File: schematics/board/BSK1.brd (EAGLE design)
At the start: 82 x 100 mm, 70 parts

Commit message: Исправлена БСК1
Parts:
- added R24, R25: 2k26, resistor:R0603
- R1, R2: value 2k26 -> 200k
- R3, R5: value 1M -> 100R
- R4, R7: value 2M -> 100k
- moved R1 2.40 mm to (66.8, 51.1)
- moved R2 2.40 mm to (66.8, 53.5)
- moved U$57 0.32 mm to (58.6, 3.20), turned to 270 degrees
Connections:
- new net N$25: R1.2, R24.1, U$22.1
- new net N$26: R2.2, R25.1, U$22.3
- net 3V3: now also U$57.4, U$57.7; no longer U$57.5
- net B1-KVCC: now also R24.2, R25.2; no longer R1.2, R2.2, U$22.1, U$22.3
- net GND: now also U$57.3, U$57.8; no longer U$57.1, U$57.2, U$57.6
- net N$150: now also U$57.1; no longer U$57.8
- net N$151: now also U$57.2; no longer U$57.7
- net SCL-INA: now also U$57.5; no longer U$57.4
- net SDA-INA: now also U$57.6; no longer U$57.3
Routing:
- net 3V3: track 183.2 -> 197.9 mm, vias 7 -> 9
- net N$25: track 0.00 -> 13.2 mm
- net GND: track 69.4 -> 59.0 mm, vias 2 -> 0
- net N$26: track 0.00 -> 4.90 mm
- net B1-KVCC: track 85.9 -> 81.1 mm
- net SCL-INA: track 11.2 -> 8.40 mm
- net SP+: track 35.1 -> 33.1 mm, vias 0 -> 1
- net N$151: track 5.94 -> 7.75 mm
- net PL5-KVCC: track 128.9 -> 130.5 mm
- net SDA-INA: track 7.90 -> 6.74 mm
- net N$150: track 5.59 -> 6.15 mm

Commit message: Плата АB+DC-DC
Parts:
- moved R3 1.10 mm to (72.3, 54.2)
- moved R4 1.10 mm to (75.5, 62.6)
- moved R5 1.10 mm to (72.3, 65.5)
- moved R7 1.10 mm to (75.5, 56.1)
- moved U$17 1.10 mm to (72.3, 59.4)
- moved U$2 0.65 mm to (21.6, 69.4)
- moved U$4 0.65 mm to (60.4, 69.4)
- moved U$19 0.65 mm to (21.6, 30.6)
- moved U$21 0.65 mm to (60.4, 30.6)
- moved U$3 0.65 mm to (68.9, 77.9)
- moved U$1 0.65 mm to (13.1, 77.9)
- moved U$20 0.65 mm to (68.9, 22.1)
- moved U$18 0.65 mm to (13.1, 22.1)
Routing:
- net BUS+: track 313.6 -> 355.4 mm, vias 6 -> 10
- net 5V: track 377.0 -> 393.7 mm
- net SP-: track 134.3 -> 140.5 mm
- net PL4-GND: track 32.4 -> 36.3 mm, vias 1 -> 3
- net SP+: track 33.1 -> 36.7 mm
- net SP-3: track 18.7 -> 22.1 mm
- net SP+2: track 19.2 -> 22.5 mm
- net SP+3: track 19.2 -> 22.5 mm
- net SP-1: track 19.2 -> 22.5 mm
- net SP-2: track 19.2 -> 22.5 mm
- net BMS2: track 79.0 -> 76.4 mm, vias 1 -> 2
- net SP+1: track 19.2 -> 21.8 mm
- net B1-CMD: track 143.7 -> 145.9 mm
- net PL3-KVCC: track 70.6 -> 72.6 mm
- net PL3: track 70.8 -> 72.7 mm
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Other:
- outline, holes or cut-outs redrawn

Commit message: Изменен номинал резисторов
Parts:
- R19: value 1k5 -> 3k3
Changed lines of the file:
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@@
 <attribute name="NAME" x="13.2712" y="35.5838" size="1.27" layer="25" ratio="10" rot="R90"/>
 </element>
-<element name="R19" library="resistor" package="R0603" package3d_urn="urn:adsk.eagle:package:23555/3" value="1k5" x="11.5" y="38.7" smashed="yes">
+<element name="R19" library="resistor" package="R0603" package3d_urn="urn:adsk.eagle:package:23555/3" value="3k3" x="11.5" y="38.7" smashed="yes">
 <attribute name="NAME" x="10.865" y="39.335" size="1.27" layer="25"/>
 <attribute name="VALUE" x="10.865" y="36.795" size="1.27" layer="27"/>

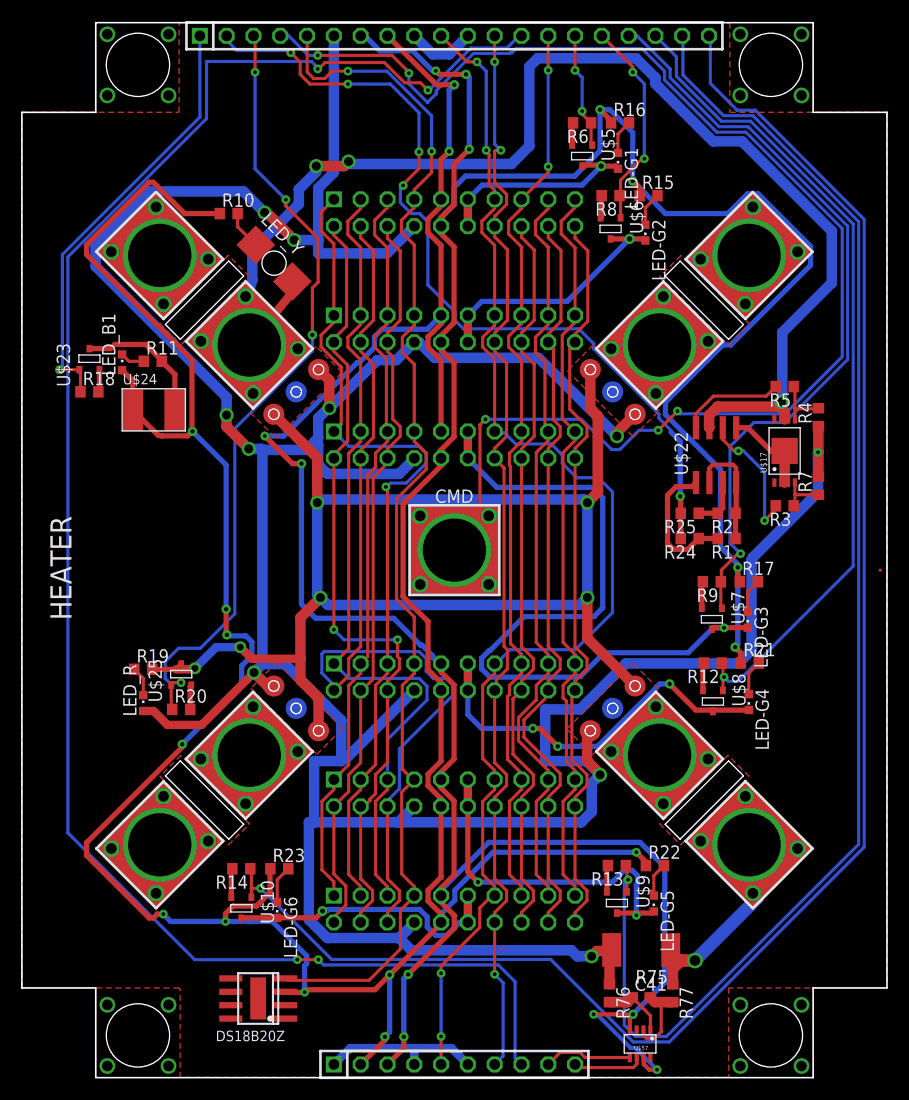
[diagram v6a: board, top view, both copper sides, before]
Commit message: Выполнена перетрассировка платы BSK1. Осталось нанести маркировку
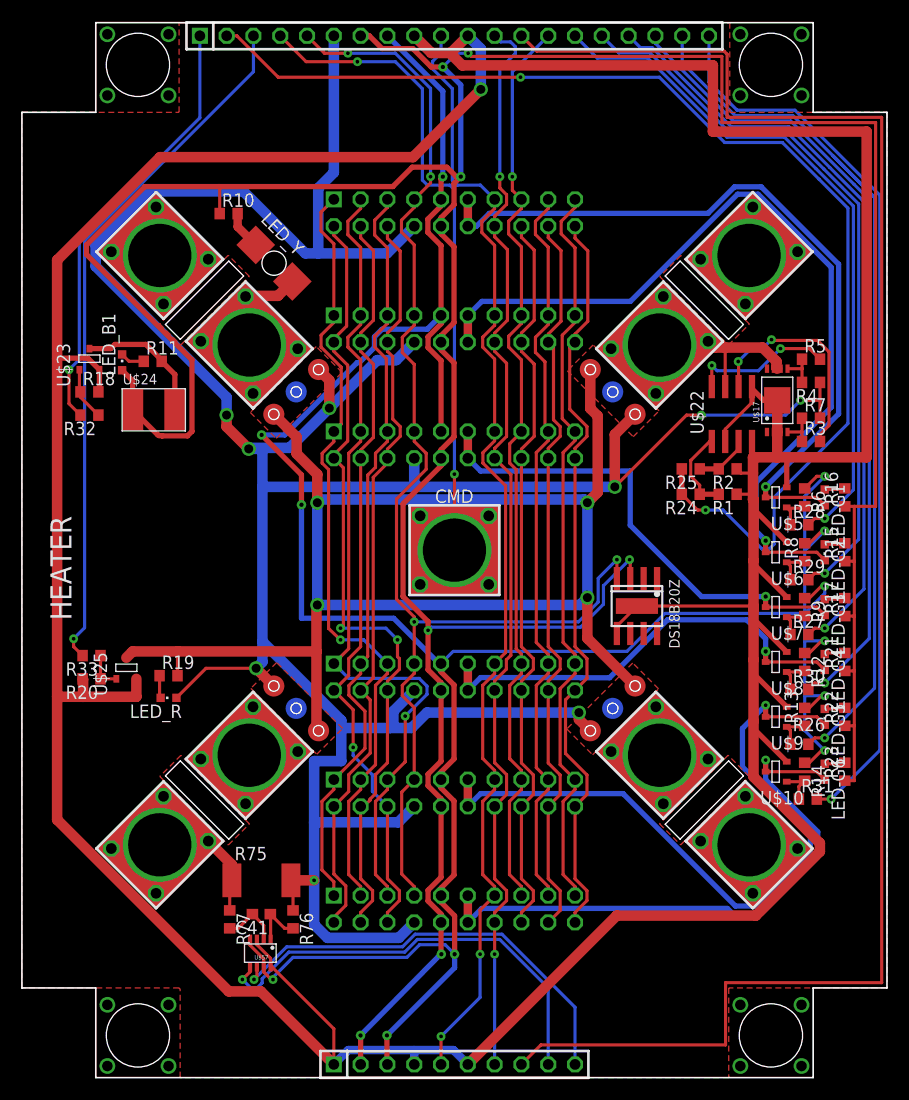
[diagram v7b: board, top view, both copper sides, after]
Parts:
- added R26, R27, R28, R29, R30, R31, R32, R33: 100R, resistor:R0603
- moved R23 54.4 mm to (78.0, 29.0), turned to 90 degrees
- moved R14 54.2 mm to (74.2, 29.0), turned to 270 degrees
- moved LED-G6 53.5 mm to (76.1, 29.0)
- moved U$10 52.3 mm to (71.5, 29.0), turned to 90 degrees
- moved DS18B20Z 51.7 mm to (58.3, 44.7), turned to 180 degrees
- moved R77 42.6 mm to (19.7, 15.0)
- moved R16 41.4 mm to (78.0, 55.0), turned to 90 degrees
- moved R6 41.3 mm to (74.2, 55.0), turned to 270 degrees
- moved R15 38.6 mm to (78.0, 49.8), turned to 90 degrees
- moved R8 38.5 mm to (74.2, 49.8), turned to 90 degrees
- moved LED-G1 37.4 mm to (76.1, 55.0)
- moved U$5 37.3 mm to (71.5, 55.0), turned to 90 degrees
- moved U$57 37.0 mm to (22.6, 11.8)
- moved C41 36.9 mm to (22.7, 15.5), turned to 180 degrees
- moved R75 36.6 mm to (22.7, 18.7), turned to 0 degrees
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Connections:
- new net N$29: R13.1, R26.1, U$9.1
- new net N$30: R27.1, R9.2, U$7.1
- new net N$31: R28.1, R6.2, U$5.1
- new net N$32: R14.2, R31.1, U$10.1
- new net N$34: R29.1, R8.1, U$6.1
- new net N$35: R12.2, R30.1, U$8.1
- new net N$36: R18.1, R32.1, U$23.1
- new net N$37: R20.1, R33.1, U$25.1
- net 3V3: now also R12.1, R13.2, R14.1, R6.1, R8.2, R9.1
- net B1-KHEAT: now also R32.2; no longer R18.1, U$23.1
- net B1-ROZE: now also R33.2; no longer R20.1, U$25.1
- net GND: no longer R12.2, R13.2, R14.2, R6.2, R8.2, R9.2
- net PL1-KVCC: now also R28.2; no longer R6.1, U$5.1
- net PL2-KVCC: now also R29.2; no longer R8.1, U$6.1
- net PL3-KVCC: now also R27.2; no longer R9.1, U$7.1
- net PL4-KVCC: now also R30.2; no longer R12.1, U$8.1
- net PL5-KVCC: now also R26.2; no longer R13.1, U$9.1
- net PL6-KVCC: now also R31.2; no longer R14.1, U$10.1
- net SP+: no longer R75.1, R77.1
- net SP+3: now also R75.1, R77.1
- net SP-: no longer U$17.67, U$22.7
- net SP-1: now also U$17.67, U$22.7
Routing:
- net GND: track 60.7 -> 429.5 mm, vias 0 -> 1
- net SP-: track 140.5 -> 24.1 mm, vias 3 -> 0
- net PL6-KVCC: track 158.5 -> 85.5 mm
- net B1-CMD: track 145.9 -> 80.2 mm, vias 5 -> 2
- net 5V: track 393.7 -> 332.1 mm, vias 17 -> 7
- net BUS+: track 355.4 -> 297.9 mm, vias 10 -> 9
- net PL2-GND: track 24.2 -> 80.9 mm
- net 3V3: track 197.9 -> 253.3 mm, vias 9 -> 12
- net PL1-KVCC: track 11.0 -> 65.6 mm, vias 2 -> 1
- net PL1-GND: track 20.1 -> 73.1 mm
- net PL2-KVCC: track 20.1 -> 69.1 mm, vias 2 -> 1
- net PL5-KVCC: track 132.2 -> 86.6 mm
- net SDA-INA: track 6.74 -> 41.8 mm, vias 0 -> 1
- net SCL-INA: track 8.40 -> 42.1 mm, vias 0 -> 1
- net PL5-GND: track 33.5 -> 66.7 mm, vias 2 -> 1
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
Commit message: Две линии i2c на платах БСК заменены на одну
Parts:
- BSK5: device pinheadCS:1X10 -> pinheadCS:1X08
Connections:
- removed net SCL-INA: BSK5.9, U$57.5
- removed net SDA-INA: BSK5.10, U$57.6
- net SCL-TM: now also U$57.5
- net SDA-TM: now also U$57.6
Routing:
- net SCL-INA: track 42.1 -> 0.00 mm, vias 1 -> 0
- net SDA-INA: track 41.8 -> 0.00 mm, vias 1 -> 0
- net SDA-TM: track 105.3 -> 133.0 mm, vias 2 -> 3
- net SCL-TM: track 109.3 -> 135.3 mm, vias 2 -> 3
- net GND: track 429.5 -> 432.2 mm
- net TIME-ES: track 163.7 -> 161.1 mm
- net 3V3: track 253.3 -> 252.2 mm
- net 5V: track 332.1 -> 331.0 mm
